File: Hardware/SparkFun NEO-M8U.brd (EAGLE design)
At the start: 40.6 x 33 mm, 92 parts, among them J13 U.FL, J2 Qwiic Right Angle, J4 Qwiic Right Angle, U2 3.3V

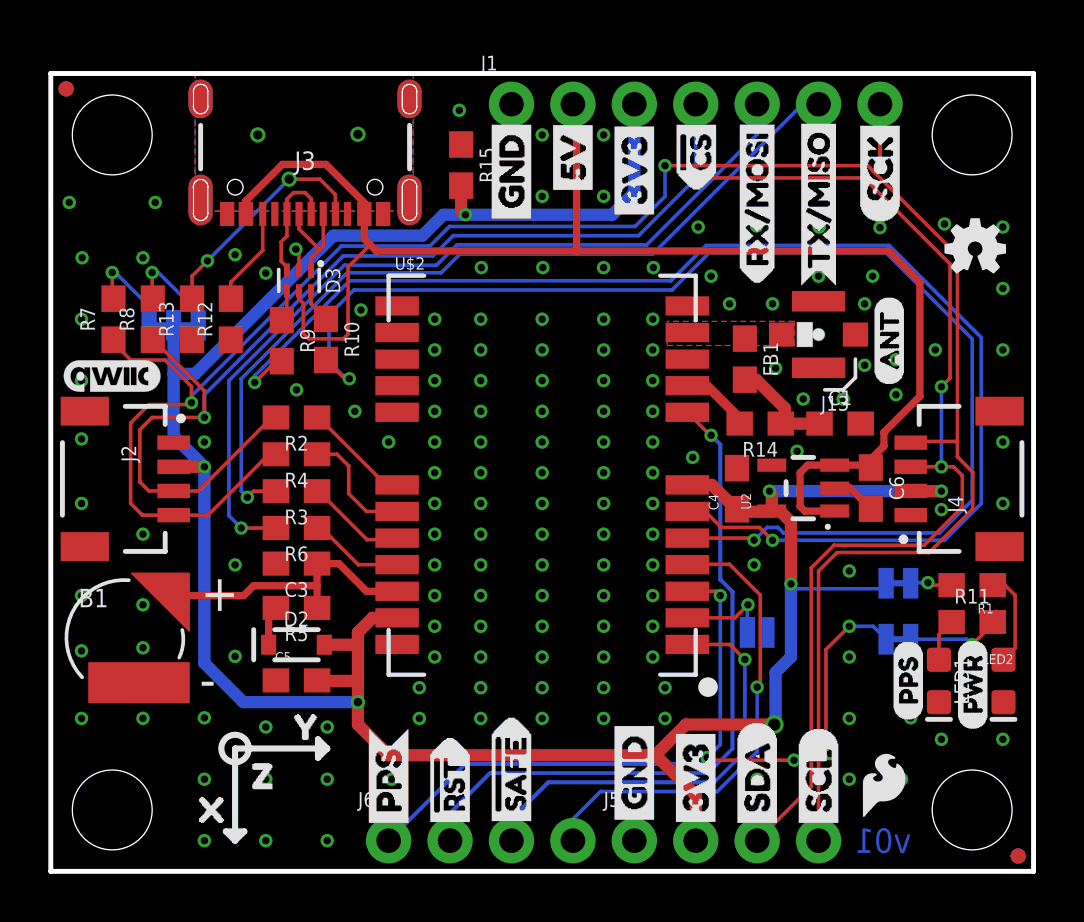
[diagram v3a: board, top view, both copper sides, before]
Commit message: Adds silk - fixes some DRC errors
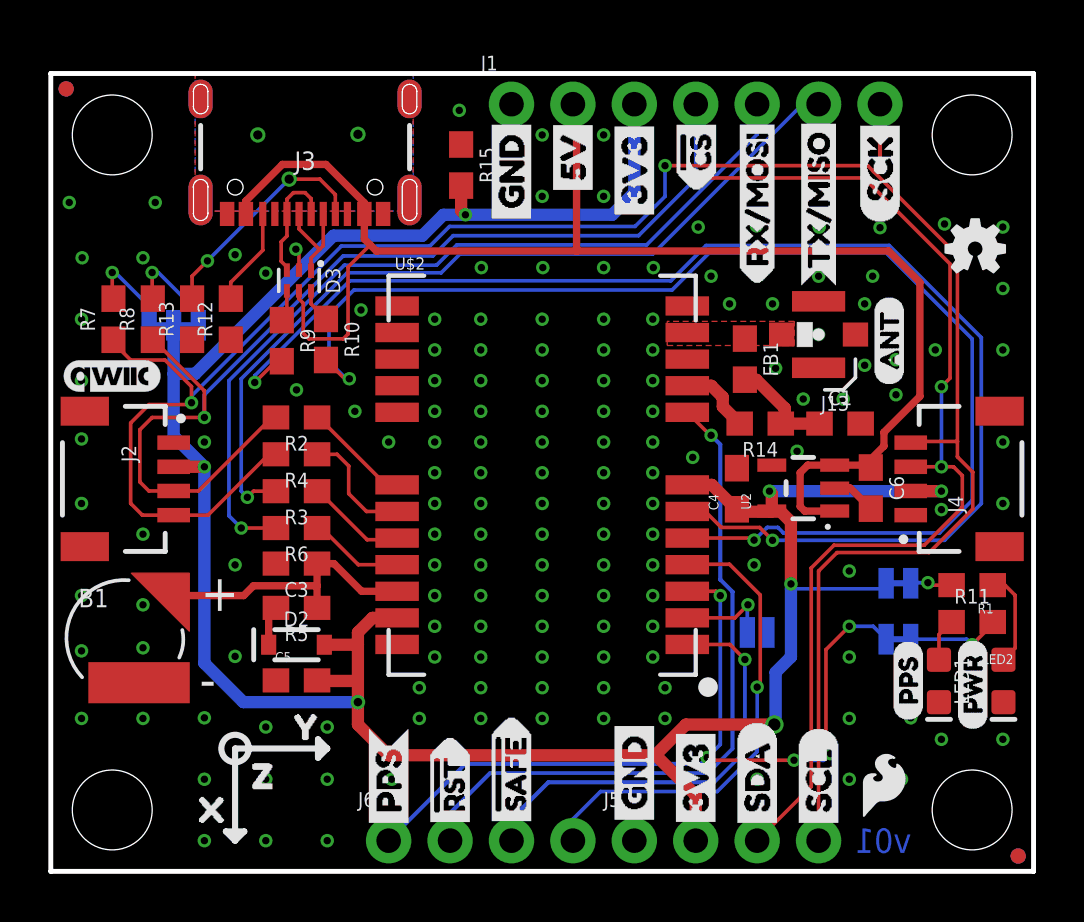
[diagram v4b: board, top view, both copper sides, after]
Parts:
- added U$15: (no value), Neo-m8u:NEO#M8U0
- added U$16: (no value), Orientation:X1
- added U$30: (no value), Orientation:Z0
- U$21: device NEO_GPS_board_silk_FINAL#03#jpg:NEO_GPS_BOARD_SILK_FINAL#03#JPG -> Orientation:Y2
- moved U$21 9.58 mm to (7.37, 5.97)
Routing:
- net N$13: track 6.03 -> 4.96 mm
- net VDD: track 2.13 -> 3.05 mm
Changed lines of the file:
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@@
 <setting verticaltext="up"/>
 </settings>
-<grid distance="0.05" unitdist="inch" unit="inch" style="lines" multiple="1" display="yes" altdistance="0.005" altunitdist="inch" altunit="inch"/>
+<grid distance="0.05" unitdist="inch" unit="inch" style="lines" multiple="1" display="yes" altdistance="0.002" altunitdist="inch" altunit="inch"/>
 <layers>
 <layer number="1" name="Top" color="4" fill="1" visible="yes" active="yes"/>
@@
 <layer number="21" name="tPlace" color="16" fill="1" visible="yes" active="yes"/>
 <layer number="22" name="bPlace" color="14" fill="1" visible="yes" active="yes"/>
-<layer number="23" name="tOrigins" color="15" fill="1" visible="no" active="yes"/>
+<layer number="23" name="tOrigins" color="15" fill="1" visible="yes" active="yes"/>
 <layer number="24" name="bOrigins" color="15" fill="1" visible="yes" active="yes"/>
 <layer number="25" name="tNames" color="7" fill="1" visible="no" active="yes"/>
@@
 <layer number="27" name="tValues" color="7" fill="1" visible="no" active="yes"/>
 <layer number="28" name="bValues" color="7" fill="1" visible="no" active="yes"/>
-<layer number="29" name="tStop" color="7" fill="3" visible="yes" active="yes"/>
+<layer number="29" name="tStop" color="7" fill="3" visible="no" active="yes"/>
 <layer number="30" name="bStop" color="7" fill="6" visible="no" active="yes"/>
 <layer number="31" name="tCream" color="7" fill="4" visible="no" active="yes"/>
@@
 <layer number="37" name="tTest" color="7" fill="1" visible="no" active="yes"/>
 <layer number="38" name="bTest" color="7" fill="1" visible="no" active="yes"/>
-<layer number="39" name="tKeepout" color="4" fill="11" visible="yes" active="yes"/>
+<layer number="39" name="tKeepout" color="4" fill="11" visible="no" active="yes"/>
 <layer number="40" name="bKeepout" color="1" fill="11" visible="no" active="yes"/>
 <layer number="41" name="tRestrict" color="4" fill="10" visible="no" active="yes"/>
@@
 <wire x1="11.049" y1="4.699" x2="11.43" y2="5.08" width="0.254" layer="21"/>
 <circle x="7.62" y="5.08" radius="0.567959375" width="0.254" layer="21"/>
+<wire x1="8.89" y1="1.27" x2="8.89" y2="5.08" width="0.254" layer="22"/>
+<wire x1="8.89" y1="5.08" x2="5.08" y2="5.08" width="0.254" layer="22"/>
+<wire x1="8.89" y1="1.27" x2="9.271" y2="1.651" width="0.254" layer="22"/>
+<wire x1="9.271" y1="1.651" x2="8.509" y2="1.651" width="0.254" layer="22"/>
+<wire x1="8.509" y1="1.651" x2="8.89" y2="1.27" width="0.254" layer="22"/>
+<wire x1="5.08" y1="5.08" x2="5.461" y2="5.461" width="0.254" layer="22"/>
+<wire x1="5.461" y1="5.461" x2="5.461" y2="4.699" width="0.254" layer="22"/>
+<wire x1="5.461" y1="4.699" x2="5.08" y2="5.08" width="0.254" layer="22"/>
+<wire x1="8.4545875" y1="5.515409375" x2="9.3526125" y2="4.617384375" width="0.254" layer="22"/>
+<wire x1="9.300009375" y1="5.464609375" x2="8.401984375" y2="4.566584375" width="0.254" layer="22"/>
 </plain>
 <attributes>
@@
 <element name="U$12" library="LEDs" package="PPS0" value="" x="36.703" y="7.747" smashed="yes" rot="MR0"/>
 <element name="U$17" library="LEDs" package="PWR1" value="" x="36.957" y="13.716" smashed="yes" rot="MR0"/>
-<element name="U$21" library="NEO_GPS_board_silk_FINAL#03#jpg" package="NEO_GPS_BOARD_SILK_FINAL#03#JPG" value="" x="15.24" y="11.43" smashed="yes" rot="MR0"/>
 <element name="U$25" library="ANT" package="ANT0" value="" x="34.671" y="20.066" smashed="yes" rot="R90"/>
 <element name="J6" library="SparkFun-Connectors" package="1X04_NO_SILK" value="" x="13.97" y="1.27" smashed="yes">
@@
 <element name="U$26" library="buzzard_labels (36)" package="RX#MOSI3" value="" x="29.21" y="24.2316" smashed="yes" rot="R90"/>
 <element name="U$29" library="buzzard_labels (36)" package="TX#MISO1" value="" x="31.75" y="24.13" smashed="yes" rot="R90"/>
+<element name="U$15" library="Neo-m8u" package="NEO#M8U0" value="" x="27.432" y="15.113" smashed="yes" rot="MR0"/>
+<element name="U$16" library="Orientation" package="X1" value="" x="11.303" y="2.54" smashed="yes" rot="MR0"/>
+<element name="U$21" library="Orientation" package="Y2" value="" x="7.366" y="5.969" smashed="yes" rot="MR0"/>
+<element name="U$30" library="Orientation" package="Z0" value="" x="9.144" y="3.937" smashed="yes" rot="MR0"/>
 </elements>
 <signals>
@@
 <wire x1="25.019" y1="4.8006" x2="26.67" y2="3.1496" width="0.508" layer="1"/>
 <wire x1="13.97" y1="4.8006" x2="25.019" y2="4.8006" width="0.508" layer="1"/>
-<wire x1="12.7" y1="9.8806" x2="13.3024" y2="10.483" width="0.508" layer="1"/>
-<wire x1="12.7" y1="9.8806" x2="12.7" y2="9.3726" width="0.508" layer="1"/>
+<wire x1="12.7" y1="9.3726" x2="12.7" y2="9.8806" width="0.508" layer="1"/>
 <wire x1="12.7" y1="9.3726" x2="12.7" y2="7.874" width="0.508" layer="1"/>
 <wire x1="12.7" y1="7.874" x2="12.7" y2="6.9986" width="0.508" layer="1"/>
@@
 <contactref element="R15" pad="2"/>
 <contactref element="U$2" pad="7"/>
-<wire x1="13.3024" y1="10.483" x2="14.32" y2="10.483" width="0.508" layer="1"/>
 <wire x1="28.3718" y1="14.9742" x2="28.3464" y2="14.9742" width="0.508" layer="1"/>
 <wire x1="28.3464" y1="14.9742" x2="27.3376" y2="15.983" width="0.508" layer="1"/>
 <wire x1="27.3376" y1="15.983" x2="26.32" y2="15.983" width="0.508" layer="1"/>
 <wire x1="16.9672" y1="27.3304" x2="16.9672" y2="28.36" width="0.508" layer="1"/>
-<wire x1="12.7" y1="6.0706" x2="12.7" y2="6.9206" width="0.508" layer="1"/>
 <wire x1="7.962" y1="6.9986" x2="12.7" y2="6.9986" width="0.508" layer="16"/>
 <via x="12.7" y="6.9986" extent="1-16" drill="0.35"/>
@@
 <wire x1="11.01" y1="7.8994" x2="11.0354" y2="7.874" width="0.508" layer="1"/>
 <wire x1="11.0354" y1="7.874" x2="12.7" y2="7.874" width="0.508" layer="1"/>
-<wire x1="12.7" y1="6.9986" x2="12.7" y2="6.9206" width="0" layer="19" extent="1-1"/>
+<wire x1="12.7" y1="9.8806" x2="13.3024" y2="10.483" width="0.508" layer="1"/>
+<wire x1="13.3024" y1="10.483" x2="14.32" y2="10.483" width="0.508" layer="1"/>
+<wire x1="12.7" y1="6.0706" x2="12.7" y2="6.9986" width="0.508" layer="1"/>
 </signal>
 <signal name="GND">
@@
 <contactref element="U$2" pad="18"/>
 <contactref element="R2" pad="1"/>
-<wire x1="11.01" y1="18.7706" x2="11.4554" y2="18.7706" width="0.1524" layer="1"/>
 <wire x1="11.01" y1="18.7706" x2="11.0744" y2="18.7706" width="0.1524" layer="1"/>
 <wire x1="11.0744" y1="18.7706" x2="13.862" y2="15.983" width="0.1524" layer="1"/>
@@
 <contactref element="U$2" pad="19"/>
 <contactref element="R4" pad="1"/>
-<wire x1="11.01" y1="17.2466" x2="11.2014" y2="17.2466" width="0.1524" layer="1"/>
-<wire x1="13.438" y1="14.883" x2="14.32" y2="14.883" width="0.1524" layer="1"/>
 <wire x1="14.32" y1="14.883" x2="13.057" y2="14.883" width="0.1524" layer="1"/>
 <wire x1="12.319" y1="15.621" x2="12.319" y2="16.764" width="0.1524" layer="1"/>
@@
 <contactref element="R5" pad="1"/>
 <wire x1="5.07" y1="11.684" x2="5.3494" y2="11.4046" width="0.3048" layer="1"/>
-<wire x1="11.01" y1="10.541" x2="11.01" y2="10.8966" width="0.3048" layer="1"/>
-<wire x1="11.9126" y1="12.7254" x2="11.01" y2="12.7254" width="0.3048" layer="1"/>
-<wire x1="12.954" y1="11.684" x2="11.9126" y2="12.7254" width="0.3048" layer="1"/>
 <wire x1="11.01" y1="12.7254" x2="11.01" y2="11.811" width="0.3048" layer="1"/>
 <wire x1="11.01" y1="11.811" x2="11.01" y2="10.8966" width="0.3048" layer="1"/>
@@
 <wire x1="5.3494" y1="11.4046" x2="7.9756" y2="11.4046" width="0.3048" layer="1"/>
 <wire x1="7.9756" y1="11.4046" x2="8.382" y2="11.811" width="0.3048" layer="1"/>
-<wire x1="14.32" y1="11.583" x2="13.055" y2="11.583" width="0.3048" layer="1"/>
-<wire x1="13.055" y1="11.583" x2="12.954" y2="11.684" width="0.3048" layer="1"/>
+<wire x1="14.32" y1="11.583" x2="12.853" y2="11.583" width="0.3048" layer="1"/>
+<wire x1="12.853" y1="11.583" x2="11.7106" y2="12.7254" width="0.3048" layer="1"/>
+<wire x1="11.7106" y1="12.7254" x2="11.01" y2="12.7254" width="0.3048" layer="1"/>
 </signal>
 <signal name="VDD">
 <contactref element="U$2" pad="9"/>
 <contactref element="R14" pad="2"/>
-<wire x1="28.487" y1="18.5166" x2="28.487" y2="18.7316" width="0.4064" layer="1"/>
-<wire x1="28.487" y1="18.7316" x2="27.1356" y2="20.083" width="0.4064" layer="1"/>
-<wire x1="27.1356" y1="20.083" x2="26.32" y2="20.083" width="0" layer="19" extent="1-1"/>
+<wire x1="28.487" y1="18.5166" x2="27.7876" y2="19.216" width="0.508" layer="1"/>
+<wire x1="27.7876" y1="19.216" x2="27.7876" y2="19.6088" width="0.508" layer="1"/>
+<wire x1="27.7876" y1="19.6088" x2="27.3134" y2="20.083" width="0.508" layer="1"/>
+<wire x1="27.3134" y1="20.083" x2="26.32" y2="20.083" width="0.508" layer="1"/>
 </signal>
 </signals>

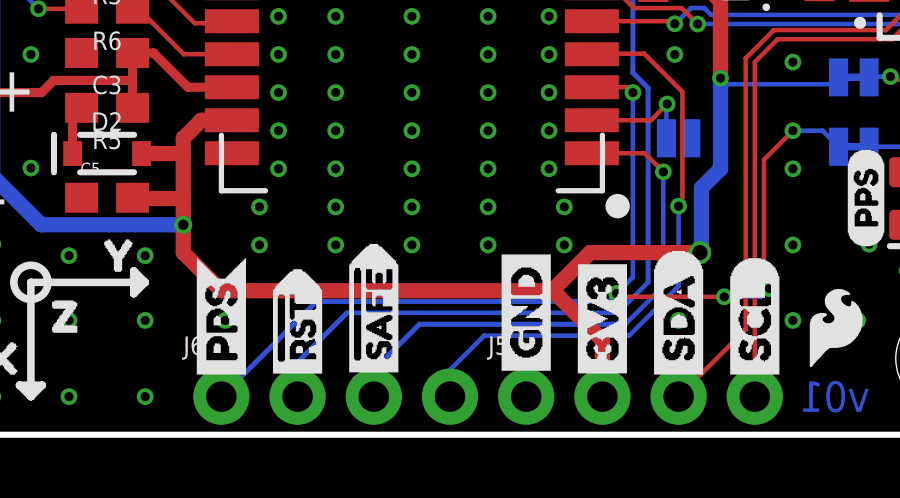
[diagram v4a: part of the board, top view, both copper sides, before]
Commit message: Adds interrupt silk
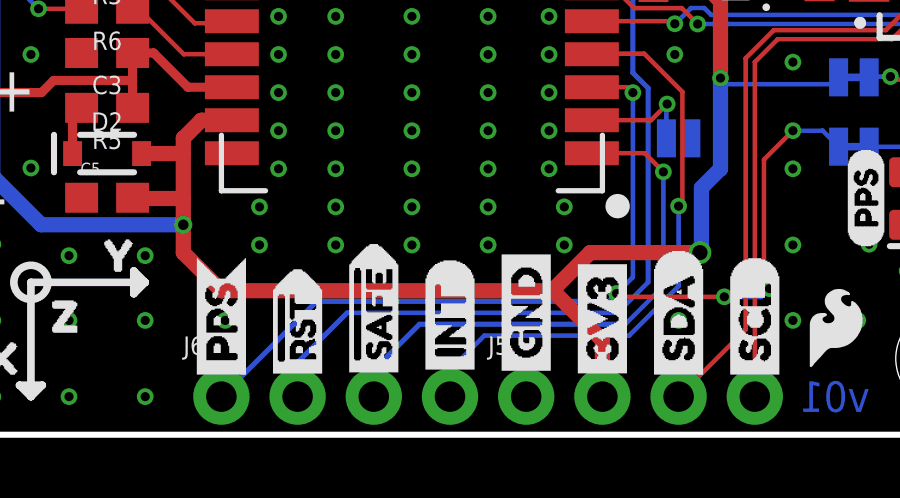
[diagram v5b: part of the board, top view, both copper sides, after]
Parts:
- added U$32, U$34: (no value), interrupt:INT0
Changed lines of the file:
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@@
 <setting verticaltext="up"/>
 </settings>
-<grid distance="0.05" unitdist="inch" unit="inch" style="lines" multiple="1" display="yes" altdistance="0.002" altunitdist="inch" altunit="inch"/>
+<grid distance="0.05" unitdist="inch" unit="inch" style="lines" multiple="1" display="yes" altdistance="0.005" altunitdist="inch" altunit="inch"/>
 <layers>
 <layer number="1" name="Top" color="4" fill="1" visible="yes" active="yes"/>
@@
 <layer number="115" name="ReferenceISLANDS" color="7" fill="1" visible="no" active="no"/>
 <layer number="116" name="Patch_BOT" color="9" fill="4" visible="no" active="no"/>
-<layer number="117" name="PM_Ref" color="26" fill="1" visible="no" active="yes"/>
+<layer number="117" name="PM_Ref" color="26" fill="1" visible="yes" active="yes"/>
 <layer number="118" name="Rect_Pads" color="7" fill="1" visible="no" active="no"/>
-<layer number="119" name="PF_Ref" color="31" fill="1" visible="no" active="yes"/>
-<layer number="120" name="WFL_Ref" color="25" fill="1" visible="no" active="yes"/>
+<layer number="119" name="PF_Ref" color="31" fill="1" visible="yes" active="yes"/>
+<layer number="120" name="WFL_Ref" color="25" fill="1" visible="yes" active="yes"/>
 <layer number="121" name="_tsilk" color="7" fill="1" visible="no" active="no"/>
 <layer number="122" name="_bsilk" color="7" fill="1" visible="no" active="no"/>
@@
 <element name="U$21" library="Orientation" package="Y2" value="" x="7.366" y="5.969" smashed="yes" rot="MR0"/>
 <element name="U$30" library="Orientation" package="Z0" value="" x="9.144" y="3.937" smashed="yes" rot="MR0"/>
+<element name="U$32" library="interrupt" package="INT0" value="" x="21.59" y="1.651" smashed="yes" rot="R90"/>
+<element name="U$34" library="interrupt" package="INT0" value="" x="21.59" y="1.651" smashed="yes" rot="MR90"/>
 </elements>
 <signals>
